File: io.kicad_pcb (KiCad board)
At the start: 2 copper layers, 145.5 x 51 mm, 83 parts, among them P1 OUT_GND, P10 INJ-CPU, P11 INJECTORS, P12 LSD-CPU, P13 LSDS, P2 TRIG-cpu, P3 DIG-CPU, P4 IN-CPU, P5 CPU_PWR, P6 TRIG-IN, P7 DIG-IN, P8 IGNITION, P9 PWR_IN, U1 LM2940, U10 BTF3080EJ, U11 BTF3080EJ, U2 MIC4469, U3 MAX9926UAEE+, U4 BTF3080EJ, U5 BTF3080EJ, U6 BTF3080EJ, U7 BTF3080EJ, U8 BTF3080EJ, U9 BTF3080EJ

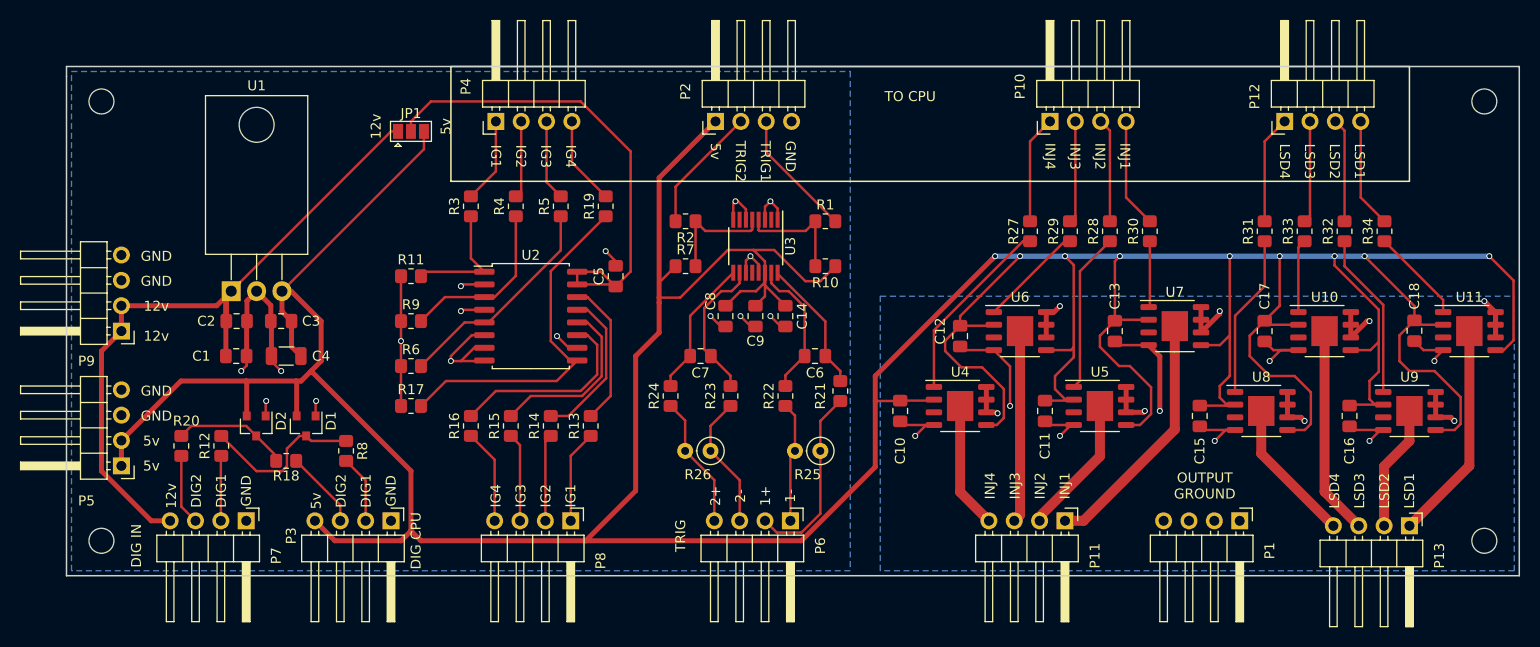
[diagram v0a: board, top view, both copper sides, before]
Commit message: Switch to a gate driver and normal power mosfets
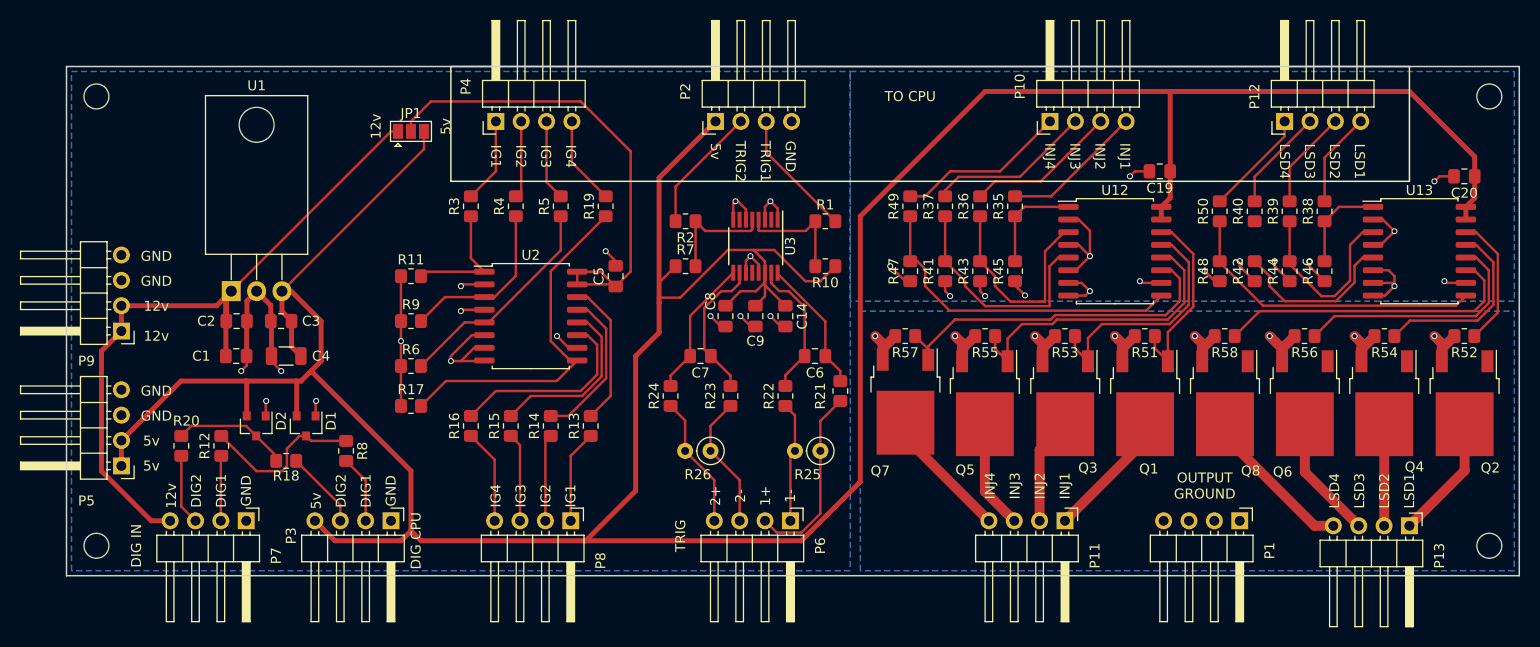
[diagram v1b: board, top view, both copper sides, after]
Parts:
- removed C10, C11, C12, C13, C15, C16, C17, C18: .1uF, Capacitor_SMD:C_0805_2012Metric_Pad1.18x1.45mm_HandSolder
- removed R27, R28, R29, R30, R31, R32, R33, R34: 1k, Resistor_SMD:R_0805_2012Metric_Pad1.20x1.40mm_HandSolder
- removed the REF** at (177.0, 109.0)
- removed the REF** at (177.0, 153.0)
- removed the REF** at (38.5, 153.0)
- removed the REF** at (38.5, 109.0)
- removed U10, U11, U4, U5, U6, U7, U8, U9: BTF3080EJ, Package_SO:Infineon_PG-DSO-8-27_3.9x4.9mm_EP2.65x3mm
- added C19: 1 uF, Capacitor_SMD:C_0805_2012Metric_Pad1.18x1.45mm_HandSolder, F.Cu at (144.5, 116.0)
- added C20: 1 uF, Capacitor_SMD:C_0805_2012Metric_Pad1.18x1.45mm_HandSolder, F.Cu at (175.0, 116.5)
- added Q1: MOSFET, Package_TO_SOT_SMD:TO-252-2, F.Cu at (143.0, 139.2)
- added Q2: MOSFET, Package_TO_SOT_SMD:TO-252-2, F.Cu at (175.0, 139.2)
- added Q3: MOSFET, Package_TO_SOT_SMD:TO-252-2, F.Cu at (135.0, 139.2)
- added Q4: MOSFET, Package_TO_SOT_SMD:TO-252-2, F.Cu at (167.0, 139.2)
- added Q5: MOSFET, Package_TO_SOT_SMD:TO-252-2, F.Cu at (127.0, 139.2)
- added Q6: MOSFET, Package_TO_SOT_SMD:TO-252-2, F.Cu at (159.0, 139.2)
- added Q7: MOSFET, Package_TO_SOT_SMD:TO-252-2, F.Cu at (119.0, 139.1)
- added Q8: MOSFET, Package_TO_SOT_SMD:TO-252-2, F.Cu at (151.0, 139.2)
- added R35: 1k, Resistor_SMD:R_0805_2012Metric_Pad1.20x1.40mm_HandSolder, F.Cu at (130.0, 119.5)
- added R36: 1k, Resistor_SMD:R_0805_2012Metric_Pad1.20x1.40mm_HandSolder, F.Cu at (126.5, 119.5)
- added R37: 1k, Resistor_SMD:R_0805_2012Metric_Pad1.20x1.40mm_HandSolder, F.Cu at (123.0, 119.5)
- added R38: 1k, Resistor_SMD:R_0805_2012Metric_Pad1.20x1.40mm_HandSolder, F.Cu at (161.0, 120.0)
- added R39: 1k, Resistor_SMD:R_0805_2012Metric_Pad1.20x1.40mm_HandSolder, F.Cu at (157.5, 120.0)
- added R40: 1k, Resistor_SMD:R_0805_2012Metric_Pad1.20x1.40mm_HandSolder, F.Cu at (154.0, 120.0)
- added R41: 100k, Resistor_SMD:R_0805_2012Metric_Pad1.20x1.40mm_HandSolder, F.Cu at (123.0, 126.0)
- added R42: 100k, Resistor_SMD:R_0805_2012Metric_Pad1.20x1.40mm_HandSolder, F.Cu at (154.0, 126.0)
- added R43: 100k, Resistor_SMD:R_0805_2012Metric_Pad1.20x1.40mm_HandSolder, F.Cu at (126.5, 126.0)
- added R44: 100k, Resistor_SMD:R_0805_2012Metric_Pad1.20x1.40mm_HandSolder, F.Cu at (157.5, 126.0)
- added R45: 100k, Resistor_SMD:R_0805_2012Metric_Pad1.20x1.40mm_HandSolder, F.Cu at (130.0, 126.0)
- added R46: 100k, Resistor_SMD:R_0805_2012Metric_Pad1.20x1.40mm_HandSolder, F.Cu at (161.0, 126.0)
- added R47: 100k, Resistor_SMD:R_0805_2012Metric_Pad1.20x1.40mm_HandSolder, F.Cu at (119.5, 126.0)
- added R48: 100k, Resistor_SMD:R_0805_2012Metric_Pad1.20x1.40mm_HandSolder, F.Cu at (150.5, 126.0)
- added R49: 1k, Resistor_SMD:R_0805_2012Metric_Pad1.20x1.40mm_HandSolder, F.Cu at (119.5, 119.5)
- added R50: 1k, Resistor_SMD:R_0805_2012Metric_Pad1.20x1.40mm_HandSolder, F.Cu at (150.5, 120.0)
- added R51: 100k, Resistor_SMD:R_0805_2012Metric_Pad1.20x1.40mm_HandSolder, F.Cu at (143.0, 132.5)
- added R52: 100k, Resistor_SMD:R_0805_2012Metric_Pad1.20x1.40mm_HandSolder, F.Cu at (175.0, 132.5)
- added R53: 100k, Resistor_SMD:R_0805_2012Metric_Pad1.20x1.40mm_HandSolder, F.Cu at (135.0, 132.5)
- added R54: 100k, Resistor_SMD:R_0805_2012Metric_Pad1.20x1.40mm_HandSolder, F.Cu at (167.0, 132.5)
- added R55: 100k, Resistor_SMD:R_0805_2012Metric_Pad1.20x1.40mm_HandSolder, F.Cu at (127.0, 132.5)
- added R56: 100k, Resistor_SMD:R_0805_2012Metric_Pad1.20x1.40mm_HandSolder, F.Cu at (159.0, 132.5)
- added R57: 100k, Resistor_SMD:R_0805_2012Metric_Pad1.20x1.40mm_HandSolder, F.Cu at (119.0, 132.5)
- added R58: 100k, Resistor_SMD:R_0805_2012Metric_Pad1.20x1.40mm_HandSolder, F.Cu at (151.0, 132.5)
- added REF**: MountingHole_2.5mm, MountingHole:MountingHole_2.5mm, F.Cu at (177.5, 108.5)
- added REF**: MountingHole_2.5mm, MountingHole:MountingHole_2.5mm, F.Cu at (177.5, 153.5)
- added REF**: MountingHole_2.5mm, MountingHole:MountingHole_2.5mm, F.Cu at (38.0, 153.5)
- added REF**: MountingHole_2.5mm, MountingHole:MountingHole_2.5mm, F.Cu at (38.0, 108.5)
- added U12: MIC4469, Package_SO:SOIC-16W_7.5x10.3mm_P1.27mm, F.Cu at (140.0, 124.0)
- added U13: MIC4469, Package_SO:SOIC-16W_7.5x10.3mm_P1.27mm, F.Cu at (170.5, 124.0)
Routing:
- net 5v: track 516.8 -> 356.1 mm, vias 9 -> 0
- net GND: track 72.1 -> 127.5 mm, vias 16 -> 32
- net OUT_GND: track 92.9 -> 45.7 mm, vias 16 -> 8
- net Net-(Q7-Pad1): track 0.00 -> 35.8 mm
- net Net-(R47-Pad2): track 0.00 -> 33.3 mm
- net Net-(R48-Pad2): track 0.00 -> 31.0 mm
- net Net-(Q8-Pad1): track 0.00 -> 30.8 mm
- net Net-(Q5-Pad1): track 0.00 -> 30.6 mm
- net Net-(Q6-Pad1): track 0.00 -> 24.9 mm
- net Net-(Q3-Pad1): track 0.00 -> 24.6 mm
- net Net-(R37-Pad1): track 0.00 -> 23.4 mm
- net Net-(R36-Pad1): track 0.00 -> 21.4 mm
- net Net-(R27-Pad1): track 19.0 -> 0.00 mm
- net Net-(Q1-Pad1): track 0.00 -> 19.0 mm
- net Net-(Q4-Pad1): track 0.00 -> 18.9 mm
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
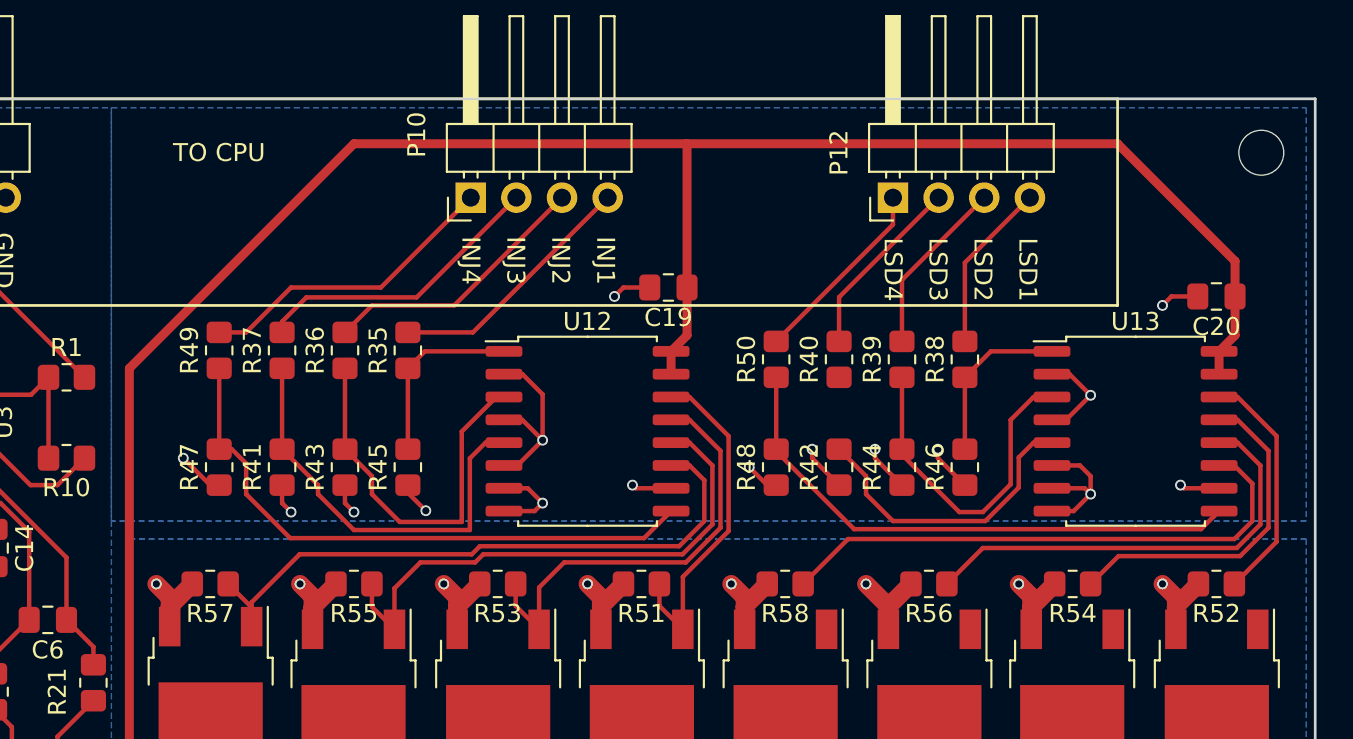
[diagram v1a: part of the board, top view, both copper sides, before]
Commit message: Post-pcb process unfuckening of basic missing traces
like a dumbass
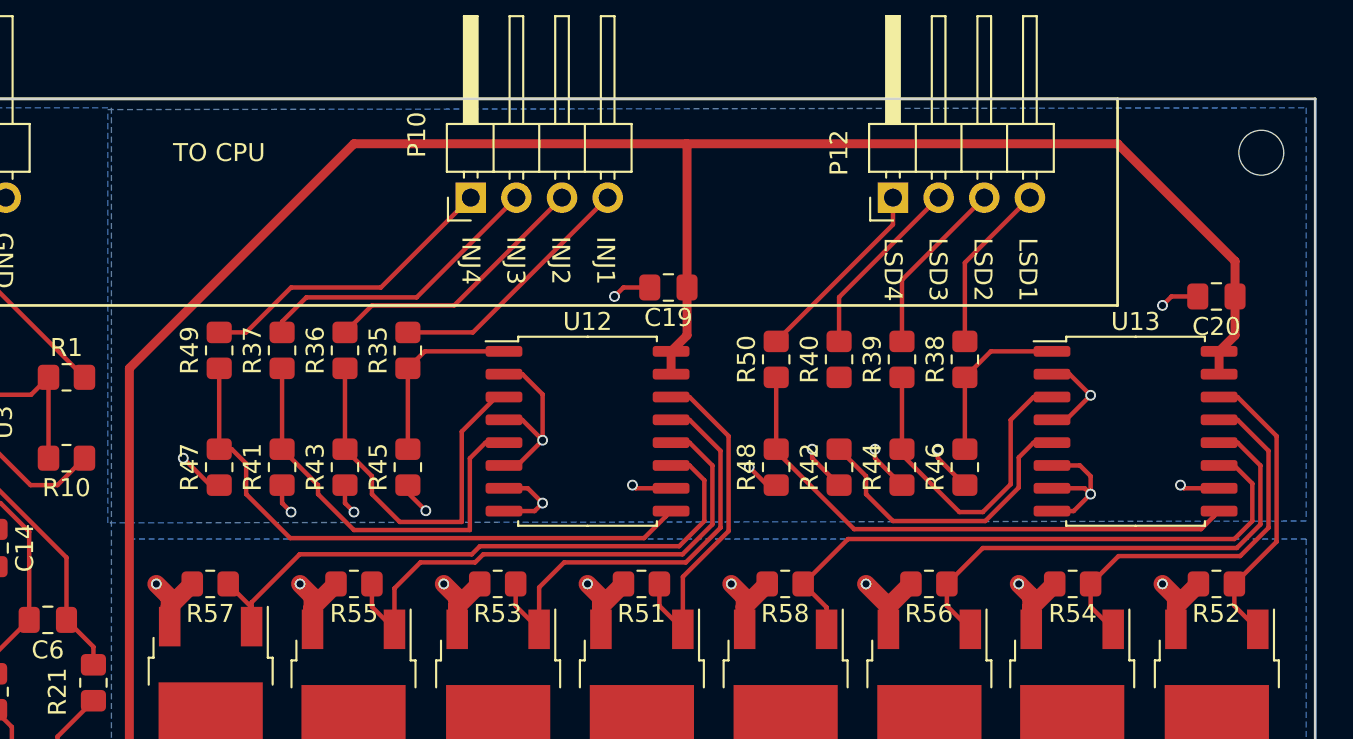
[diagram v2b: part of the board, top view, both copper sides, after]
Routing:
- net Net-(Q8-Pad1): track 30.8 -> 33.9 mm
- net Net-(Q6-Pad1): track 24.9 -> 28.0 mm
- net Net-(Q2-Pad1): track 13.3 -> 16.4 mm
- net Net-(Q4-Pad1): track 18.9 -> 22.0 mm
